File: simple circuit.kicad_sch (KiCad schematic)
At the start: 3 parts

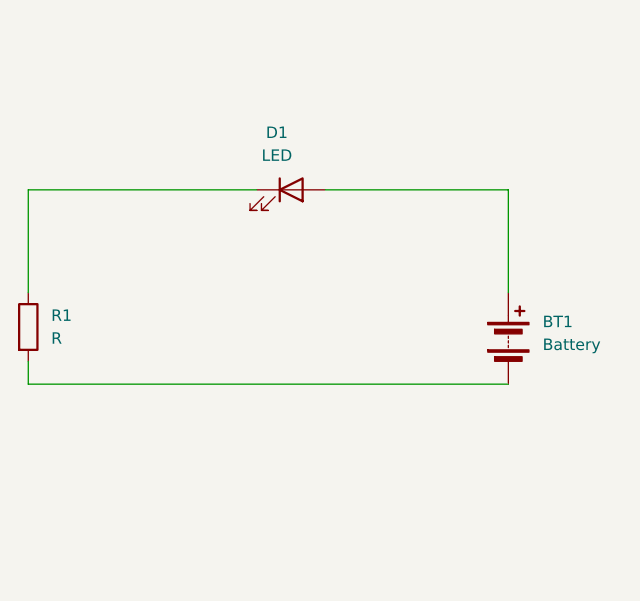
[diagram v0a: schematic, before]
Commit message: 2 battery and 2 led circuite
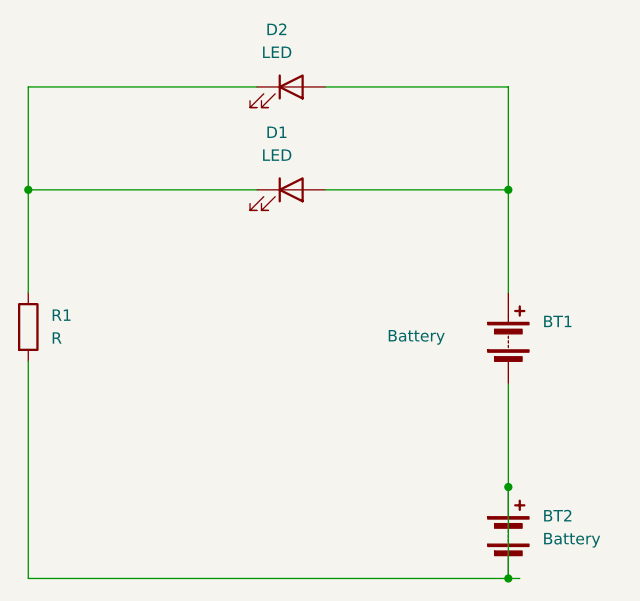
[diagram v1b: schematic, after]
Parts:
- added BT2: Battery, Battery:BatteryHolder_Keystone_500, symbol Device:Battery
- added D2: LED, LED_THT:LED_D3.0mm, symbol Device:LED
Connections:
- net at D1.1 (K), R1.1: now also D2.1 (K)
- net at BT1.2 (-), R1.2: now also BT2.1 (+), BT2.2 (-)
- net at BT1.1 (+), D1.2 (A): now also D2.2 (A)
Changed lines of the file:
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@@
 	(generator_version "9.0")
 	(paper "A4")
+	(junction
+		(at 185.42 76.2)
+		(diameter 0)
+		(color 0 0 0 0)
+	)
+	(junction
+		(at 185.42 109.22)
+		(diameter 0)
+		(color 0 0 0 0)
+	)
+	(junction
+		(at 132.08 76.2)
+		(diameter 0)
+		(color 0 0 0 0)
+	)
+	(junction
+		(at 185.42 119.38)
+		(diameter 0)
+		(color 0 0 0 0)
+	)
 	(wire
 		(pts
@@
 	(wire
 		(pts
+			(xy 185.42 97.79) (xy 185.42 109.22)
+		)
+		(stroke
+			(width 0)
+			(type default)
+		)
+	)
+	(wire
+		(pts
+			(xy 132.08 76.2) (xy 132.08 64.77)
+		)
+		(stroke
+			(width 0)
+			(type default)
+		)
+	)
+	(wire
+		(pts
 			(xy 132.08 87.63) (xy 132.08 76.2)
 		)
@@
 	(wire
 		(pts
+			(xy 185.42 119.38) (xy 185.42 109.22)
+		)
+		(stroke
+			(width 0)
+			(type default)
+		)
+	)
+	(wire
+		(pts
 			(xy 132.08 76.2) (xy 157.48 76.2)
 		)
@@
 	(wire
 		(pts
+			(xy 132.08 64.77) (xy 157.48 64.77)
+		)
+		(stroke
+			(width 0)
+			(type default)
+		)
+	)
+	(wire
+		(pts
 			(xy 185.42 76.2) (xy 185.42 87.63)
 		)
@@
 	(wire
 		(pts
-			(xy 132.08 97.79) (xy 132.08 95.25)
-		)
-		(stroke
-			(width 0)
-			(type default)
-		)
-	)
-	(wire
-		(pts
-			(xy 185.42 97.79) (xy 132.08 97.79)
+			(xy 132.08 119.38) (xy 132.08 95.25)
+		)
+		(stroke
+			(width 0)
+			(type default)
+		)
+	)
+	(wire
+		(pts
+			(xy 186.69 119.38) (xy 185.42 119.38)
+		)
+		(stroke
+			(width 0)
+			(type default)
+		)
+	)
+	(wire
+		(pts
+			(xy 185.42 64.77) (xy 185.42 76.2)
+		)
+		(stroke
+			(width 0)
+			(type default)
+		)
+	)
+	(wire
+		(pts
+			(xy 132.08 119.38) (xy 185.42 119.38)
+		)
+		(stroke
+			(width 0)
+			(type default)
+		)
+	)
+	(wire
+		(pts
+			(xy 165.1 64.77) (xy 185.42 64.77)
 		)
 		(stroke
@@
 	)
 	(symbol
+		(lib_id "Device:LED")
+		(at 161.29 64.77 0)
+		(unit 1)
+		(exclude_from_sim no)
+		(in_bom yes)
+		(on_board yes)
+		(dnp no)
+		(fields_autoplaced yes)
+		(property "Reference" "D2"
+			(at 159.7025 58.42 0)
+			(effects
+				(font
+					(size 1.27 1.27)
+				)
+			)
+		)
+		(property "Value" "LED"
+			(at 159.7025 60.96 0)
+			(effects
+				(font
+					(size 1.27 1.27)
+				)
+			)
+		)
+		(property "Footprint" "LED_THT:LED_D3.0mm"
+			(at 161.29 64.77 0)
+			(effects
+				(font
+					(size 1.27 1.27)
+				)
+				(hide yes)
+			)
+		)
+		(property "Datasheet" "~"
+			(at 161.29 64.77 0)
+			(effects
+				(font
+					(size 1.27 1.27)
+				)
+				(hide yes)
+			)
+		)
+		(property "Description" "Light emitting diode"
+			(at 161.29 64.77 0)
+			(effects
+				(font
+					(size 1.27 1.27)
+				)
+				(hide yes)
+			)
+		)
+		(property "Sim.Pins" "1=K 2=A"
+			(at 161.29 64.77 0)
+			(effects
+				(font
+					(size 1.27 1.27)
+				)
+				(hide yes)
+			)
+		)
+		(pin "1"
+		)
+		(pin "2"
+		)
+		(instances
+			(project "simple circuit"
+				(path "/bdedcdfc-a843-4f9e-b50c-3bf99662e17d"
+					(reference "D2")
+					(unit 1)
+				)
+			)
+		)
+	)
+	(symbol
+		(lib_id "Device:Battery")
+		(at 185.42 114.3 0)
+		(unit 1)
+		(exclude_from_sim no)
+		(in_bom yes)
+		(on_board yes)
+		(dnp no)
+		(fields_autoplaced yes)
+		(property "Reference" "BT2"
+			(at 189.23 112.4584 0)
+			(effects
+				(font
+					(size 1.27 1.27)
+				)
+				(justify left)
+			)
+		)
+		(property "Value" "Battery"
+			(at 189.23 114.9984 0)
+			(effects
+				(font
+					(size 1.27 1.27)
+				)
+				(justify left)
+			)
+		)
+		(property "Footprint" "Battery:BatteryHolder_Keystone_500"
+			(at 185.42 112.776 90)
+			(effects
+				(font
+					(size 1.27 1.27)
+				)
+				(hide yes)
+			)
+		)
+		(property "Datasheet" "~"
+			(at 185.42 112.776 90)
+			(effects
+				(font
+					(size 1.27 1.27)
+				)
+				(hide yes)
+			)
+		)
+		(property "Description" "Multiple-cell battery"
+			(at 185.42 114.3 0)
+			(effects
+				(font
+					(size 1.27 1.27)
+				)
+				(hide yes)
+			)
+		)
+		(pin "2"
+		)
+		(pin "1"
+		)
+		(instances
+			(project "simple circuit"
+				(path "/bdedcdfc-a843-4f9e-b50c-3bf99662e17d"
+					(reference "BT2")
+					(unit 1)
+				)
+			)
+		)
+	)
+	(symbol
 		(lib_id "Device:Battery")
 		(at 185.42 92.71 0)
@@
 		(on_board yes)
 		(dnp no)
-		(fields_autoplaced yes)
 		(property "Reference" "BT1"
 			(at 189.23 90.8684 0)
@@
 		)
 		(property "Value" "Battery"
-			(at 189.23 93.4084 0)
-			(effects
-				(font
+			(at 171.958 92.456 0)
+			(effects
+				(font
